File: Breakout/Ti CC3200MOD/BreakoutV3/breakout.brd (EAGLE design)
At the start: 52.6 x 40.5 mm, 29 parts, among them U1 TPS63001DRCT, U11 XL

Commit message: added accelormeter
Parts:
- removed JTAG: (no value), con-lstb:MA06-1
- removed R7: 100K, SparkFun-Resistors:0603-RES
- removed R8: 470K, SparkFun-Resistors:0603-RES
- added C2: 0.1uF, microbuilder:0402
- added C3, C4: .1uF, rcl:C0603
- added JP2: (no value), DECADE-libraries:1X02
- added R1, R2, R4: 33K, microbuilder:0402
- added U$1: BMA220, bma220:BMA222
- added U2: MAX17048, Maxim_By_element14_Batch_1:DFN200X200X80-9N
- moved C8 1.78 mm to (51.5, 32.3)
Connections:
- removed net JTAG_TCK: CC3200MOD.P21, JTAG.5
- removed net JTAG_TMS: CC3200MOD.P22, JTAG.6
- removed net N$15: CC3200MOD.P3, U11.GPIO_10
- removed net N$16: CC3200MOD.P4, U11.GPIO_11
- removed net N$23: CC3200MOD.P54, U11.GPIO_09
- new net GPIO_09: CC3200MOD.P54, U11.GPIO_09, U2.5
- new net GPIO_13: R4.1
- new net I2C_SCL: CC3200MOD.P3, R2.1, U$1.P12, U11.GPIO_10, U2.7
- new net I2C_SDA: CC3200MOD.P4, R1.1, U$1.P2, U11.GPIO_11, U2.8
- new net N$7: R4.2, U$1.P5
- new net OUT_JUMP: JP2.1, U$2.1, U$2.20
- net +BATT: now also C2.1, U2.2, U2.3; no longer R8.2
- net GND: now also C2.2, C3.2, C4.2, U$1.P1, U$1.P8, U$1.P9, U2.1, U2.4, U2.6; no longer JTAG.1, R7.1
- net GPIO_05: no longer R7.2, R8.1
- net JTAG_TDI: no longer JTAG.3
- net JTAG_TDO: no longer JTAG.4
- net OUT: now also JP2.2; no longer U$2.1, U$2.20
- net VCC: now also C3.1, C4.1, R1.2, R2.2, U$1.P3, U$1.P4, U$1.P7; no longer JTAG.2
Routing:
- net I2C_SDA: track 0.00 -> 91.4 mm, vias 0 -> 4
- net N$16: track 72.7 -> 0.00 mm, vias 2 -> 0
- net I2C_SCL: track 0.00 -> 72.6 mm, vias 0 -> 2
- net N$15: track 52.7 -> 0.00 mm, vias 1 -> 0
- net GPIO_09: track 0.00 -> 51.7 mm, vias 0 -> 3
- net N$23: track 44.8 -> 0.00 mm, vias 1 -> 0
- net +BATT: track 24.1 -> 62.8 mm
- net VCC: track 114.3 -> 151.1 mm, vias 1 -> 3
- net JTAG_TCK: track 23.0 -> 0.00 mm
- net JTAG_TMS: track 18.5 -> 0.00 mm, vias 1 -> 0
- net JTAG_TDI: track 76.0 -> 64.7 mm
- net JTAG_TDO: track 73.5 -> 62.5 mm
- net N$14: track 85.0 -> 74.3 mm, vias 4 -> 3
- net N$7: track 0.00 -> 7.92 mm
- net GPIO_05: track 43.2 -> 35.9 mm
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
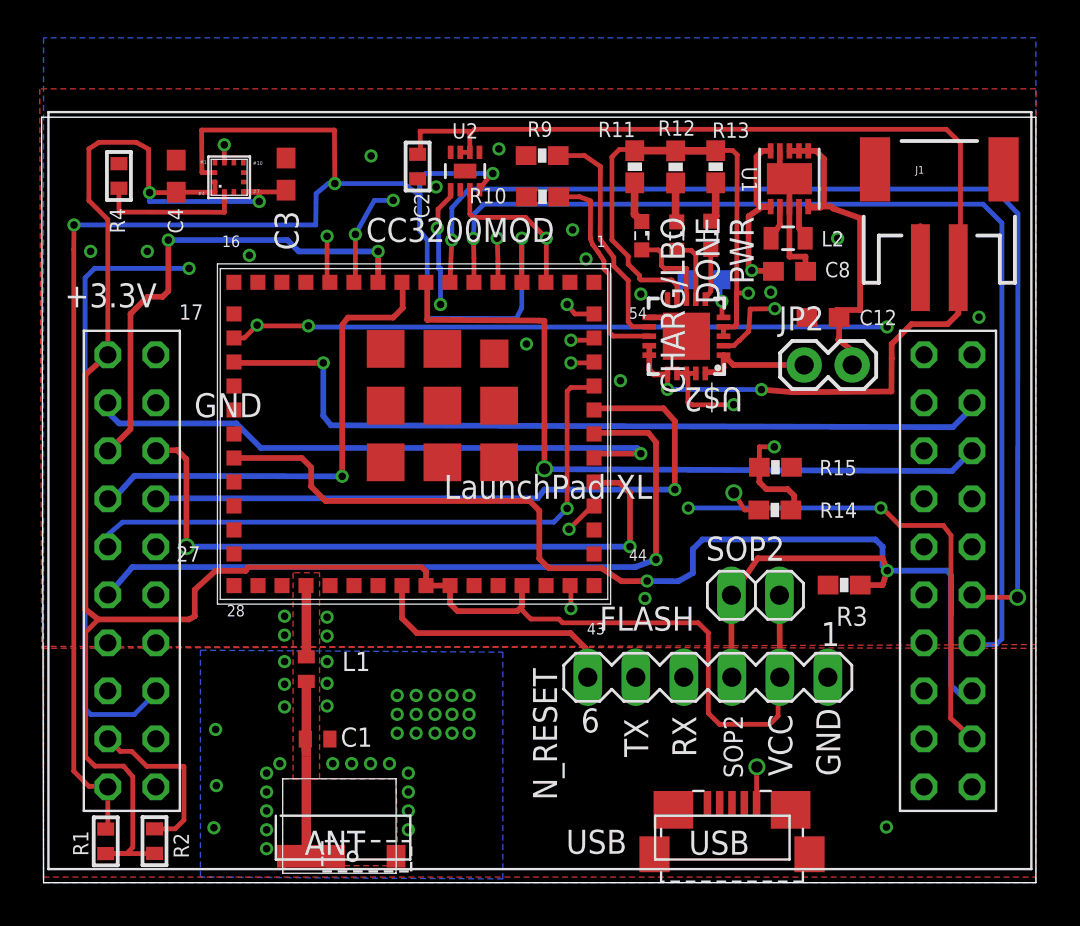
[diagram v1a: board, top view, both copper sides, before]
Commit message: Moved Micro USB and LiPo Connector to other side
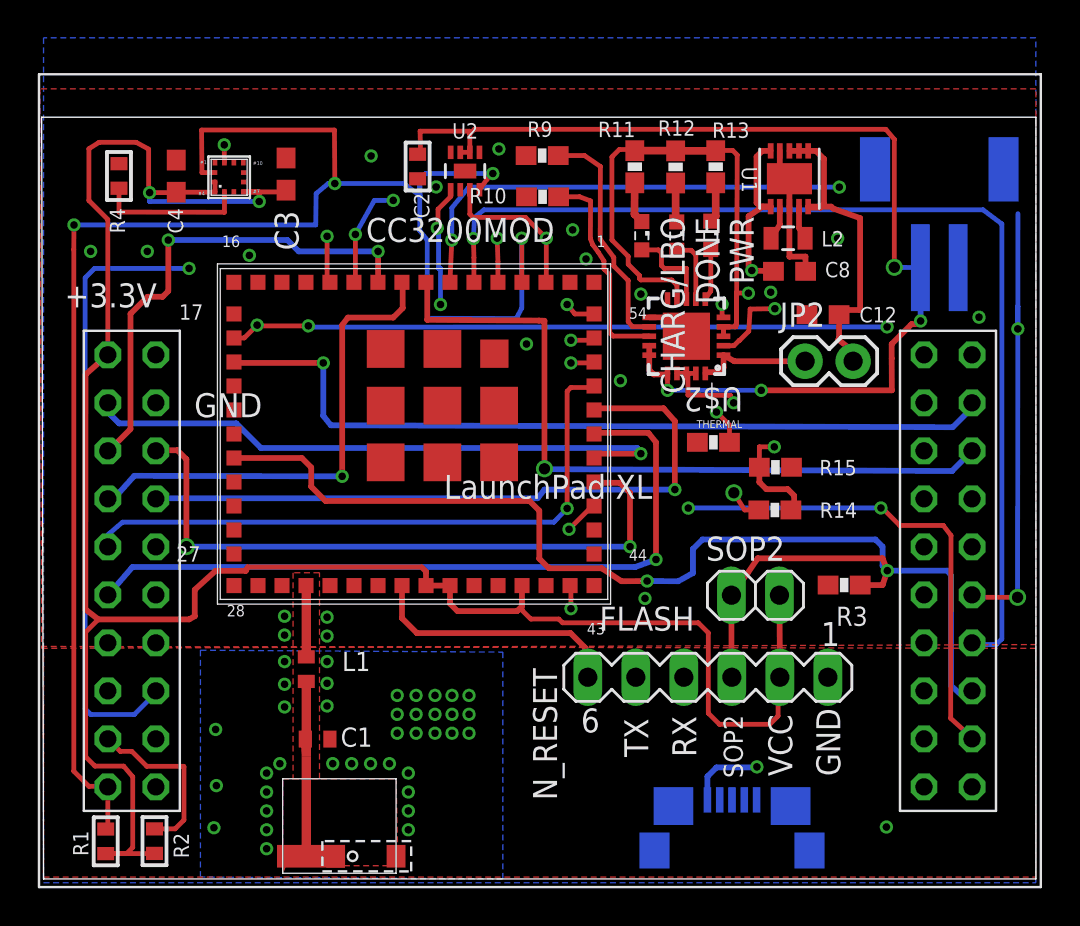
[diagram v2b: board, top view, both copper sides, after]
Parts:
- moved THERMAL 8.61 mm to (47.4, 23.3), flipped to the top, turned to 0 degrees
- moved JP2 0.21 mm to (52.3, 27.6)
- moved USB 0.20 mm to (48.4, 1.71), flipped to the bottom
- moved C12 0.15 mm to (53.2, 30.1)
- flipped J1 to the bottom
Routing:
- net N$10: track 57.6 -> 65.0 mm, vias 2 -> 4
- net N$28: track 2.18 -> 8.47 mm, vias 1 -> 2
- net +BATT: track 62.8 -> 59.1 mm, vias 2 -> 4
- net GND: track 12.2 -> 10.1 mm
- net +5V_USB: track 65.4 -> 67.3 mm
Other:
- board size 52.6 x 40.5 mm -> 52.6 x 40.3 mm
- board text added: "Breakout V3.2"

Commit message: Fixed some grounds
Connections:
- net GND: now also U2.9
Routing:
- net N$10: track 65.0 -> 57.8 mm
- net GND: track 10.1 -> 14.1 mm, vias 57 -> 59
- net I2C_SDA: track 91.4 -> 92.1 mm
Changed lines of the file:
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@@
 <wire x1="25.9" y1="15.72" x2="25.9" y2="11.95" width="0.5" layer="1"/>
 </signal>
-<signal name="GND" airwireshidden="yes">
+<signal name="GND">
 <contactref element="CC3200MOD" pad="P27"/>
 <via x="24.75" y="9.3" extent="1-16" drill="0.4"/>
@@
 <via x="43.82" y="15.04" extent="1-16" drill="0.4"/>
 <via x="37.55" y="28.5" extent="1-16" drill="0.4"/>
-<wire x1="60.39" y1="32.54" x2="60.39" y2="35.47" width="0" layer="19" extent="1-16"/>
 <via x="61.49" y="29.92" extent="1-16" drill="0.4"/>
 <contactref element="U$2" pad="10"/>
@@
 <via x="34.51" y="7.91" extent="1-16" drill="0.4"/>
 <via x="14.49" y="33.4" extent="1-16" drill="0.4"/>
-<wire x1="32.77" y1="36.81" x2="34.046" y2="36.6594" width="0" layer="19" extent="1-1"/>
-<wire x1="21.07" y1="38.095" x2="19.02" y2="38.23" width="0" layer="19" extent="1-1"/>
-<wire x1="22.595" y1="37.57" x2="21.07" y2="38.095" width="0" layer="19" extent="1-1"/>
-<wire x1="60.39" y1="32.54" x2="61.49" y2="29.92" width="0" layer="19" extent="1-1"/>
+<via x="23.26" y="39.02" extent="1-16" drill="0.4"/>
+<contactref element="U2" pad="9"/>
+<wire x1="34.046" y1="36.6594" x2="34.046" y2="37.396" width="0.254" layer="1"/>
+<wire x1="34.046" y1="37.396" x2="34.3" y2="37.65" width="0.254" layer="1"/>
+<via x="20.64" y="38.51" extent="1-16" drill="0.4"/>
+<wire x1="23.26" y1="39.02" x2="23.25" y2="39.02" width="0.254" layer="1"/>
+<wire x1="23.25" y1="39.02" x2="23.25" y2="37.56" width="0.254" layer="1"/>
+<wire x1="23.25" y1="37.56" x2="22.595" y2="37.56" width="0.254" layer="1"/>
+<wire x1="22.595" y1="37.56" x2="22.595" y2="37.57" width="0.254" layer="1"/>
+<wire x1="21.07" y1="38.095" x2="20.64" y2="38.095" width="0.254" layer="1"/>
+<wire x1="20.64" y1="38.095" x2="20.64" y2="38.51" width="0.254" layer="1"/>
 </signal>
 <signal name="N$1">
@@
 <wire x1="33.6" y1="34" x2="33.6" y2="35.7" width="0.254" layer="16"/>
 <wire x1="33.6" y1="35.7" x2="34.5" y2="36.8" width="0.254" layer="16"/>
-<wire x1="63.55" y1="35.4" x2="63.545171875" y2="30.500153125" width="0.254" layer="16"/>
 <via x="63.53" y="15.1" extent="1-16" drill="0.6"/>
-<wire x1="63.545171875" y1="30.500153125" x2="63.543990625" y2="29.30005625" width="0.254" layer="16"/>
-<wire x1="63.543990625" y1="29.30005625" x2="63.53" y2="15.1" width="0.254" layer="16"/>
+<wire x1="63.543990625" y1="30.49005625" x2="63.53" y2="15.1" width="0.254" layer="16"/>
 <wire x1="63.53" y1="15.1" x2="61.32" y2="15.1" width="0.254" layer="1"/>
 <wire x1="61.32" y1="15.1" x2="61.16" y2="15.26" width="0.254" layer="1"/>
 <wire x1="34.5" y1="36.8" x2="54.1" y2="36.8" width="0.254" layer="16"/>
 <via x="54.1" y="36.8" extent="1-16" drill="0.4"/>
-<wire x1="54.1" y1="36.8" x2="62.25" y2="36.7" width="0.254" layer="2"/>
-<wire x1="62.25" y1="36.7" x2="63.55" y2="35.4" width="0.254" layer="2"/>
-<wire x1="63.55" y1="35.4" x2="63.55" y2="29.306065625" width="0.254" layer="2"/>
-<wire x1="63.55" y1="29.306065625" x2="63.543990625" y2="29.30005625" width="0.254" layer="2"/>
-<via x="63.543990625" y="29.30005625" extent="1-16" drill="0.4"/>
-<wire x1="63.543990625" y1="29.30005625" x2="63.543990625" y2="30.498971875" width="0.254" layer="16"/>
+<wire x1="54.1" y1="36.8" x2="62.25" y2="36.8" width="0.254" layer="2"/>
+<wire x1="62.25" y1="36.8" x2="63.55" y2="35.4" width="0.254" layer="2"/>
+<wire x1="63.55" y1="35.4" x2="63.55" y2="30.476065625" width="0.254" layer="2"/>
+<wire x1="63.55" y1="30.476065625" x2="63.543990625" y2="30.49005625" width="0.254" layer="2"/>
+<via x="63.543990625" y="30.49005625" extent="1-16" drill="0.4"/>
+<wire x1="63.543990625" y1="30.49005625" x2="63.543990625" y2="30.498971875" width="0.254" layer="16"/>
 <wire x1="63.543990625" y1="30.498971875" x2="63.545171875" y2="30.500153125" width="0.254" layer="16"/>
 <wire x1="61.16" y1="15.26" x2="61.15" y2="15.26" width="0.254" layer="1"/>
@@
 <wire x1="15.4" y1="2.84" x2="15.4" y2="5.07" width="0.254" layer="1"/>
 <contactref element="U$1" pad="P2"/>
-<wire x1="21.045" y1="37.57" x2="20.38" y2="37.57" width="0.254" layer="1"/>
-<wire x1="20.38" y1="37.57" x2="20.36" y2="39.82" width="0.254" layer="1"/>
-<wire x1="20.36" y1="39.82" x2="27.39" y2="39.82" width="0.254" layer="1"/>
+<wire x1="21.045" y1="37.57" x2="20.03" y2="37.57" width="0.254" layer="1"/>
+<wire x1="20.03" y1="37.57" x2="20.01" y2="39.82" width="0.254" layer="1"/>
+<wire x1="20.01" y1="39.82" x2="27.39" y2="39.82" width="0.254" layer="1"/>
 <wire x1="27.39" y1="39.82" x2="27.41" y2="36.99" width="0.254" layer="1"/>
 <via x="27.41" y="36.99" extent="1-16" drill="0.4"/>
@@
 <wire x1="34.8" y1="39.86" x2="56.56" y2="39.86" width="0.254" layer="1"/>
 <wire x1="56.56" y1="39.86" x2="57.01" y2="39.33" width="0.254" layer="1"/>
-<wire x1="57.01" y1="39.33" x2="57.01" y2="32.56" width="0.254" layer="1"/>
-<wire x1="57.01" y1="32.56" x2="58.39" y2="32.54" width="0.254" layer="16"/>
+<wire x1="57.01" y1="39.33" x2="57" y2="32.53" width="0.254" layer="1"/>
+<wire x1="57" y1="32.53" x2="58.39" y2="32.54" width="0.254" layer="16"/>
 <contactref element="C2" pad="1"/>
 <wire x1="31.79" y1="38.54" x2="31.95" y2="38.54" width="0.254" layer="1"/>
@@
 <wire x1="34.046" y1="38.6406" x2="34.554" y2="38.6406" width="0.254" layer="1"/>
 <via x="58.4" y="29.72" extent="1-16" drill="0.4"/>
-<via x="57.01" y="32.56" extent="1-16" drill="0.6" shape="square"/>
+<via x="57" y="32.53" extent="1-16" drill="0.4"/>
 </signal>
 <signal name="N$9">
